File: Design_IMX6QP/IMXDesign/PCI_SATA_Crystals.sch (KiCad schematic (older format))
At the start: 15 parts, among them U1 MCIMX6QP5EVT

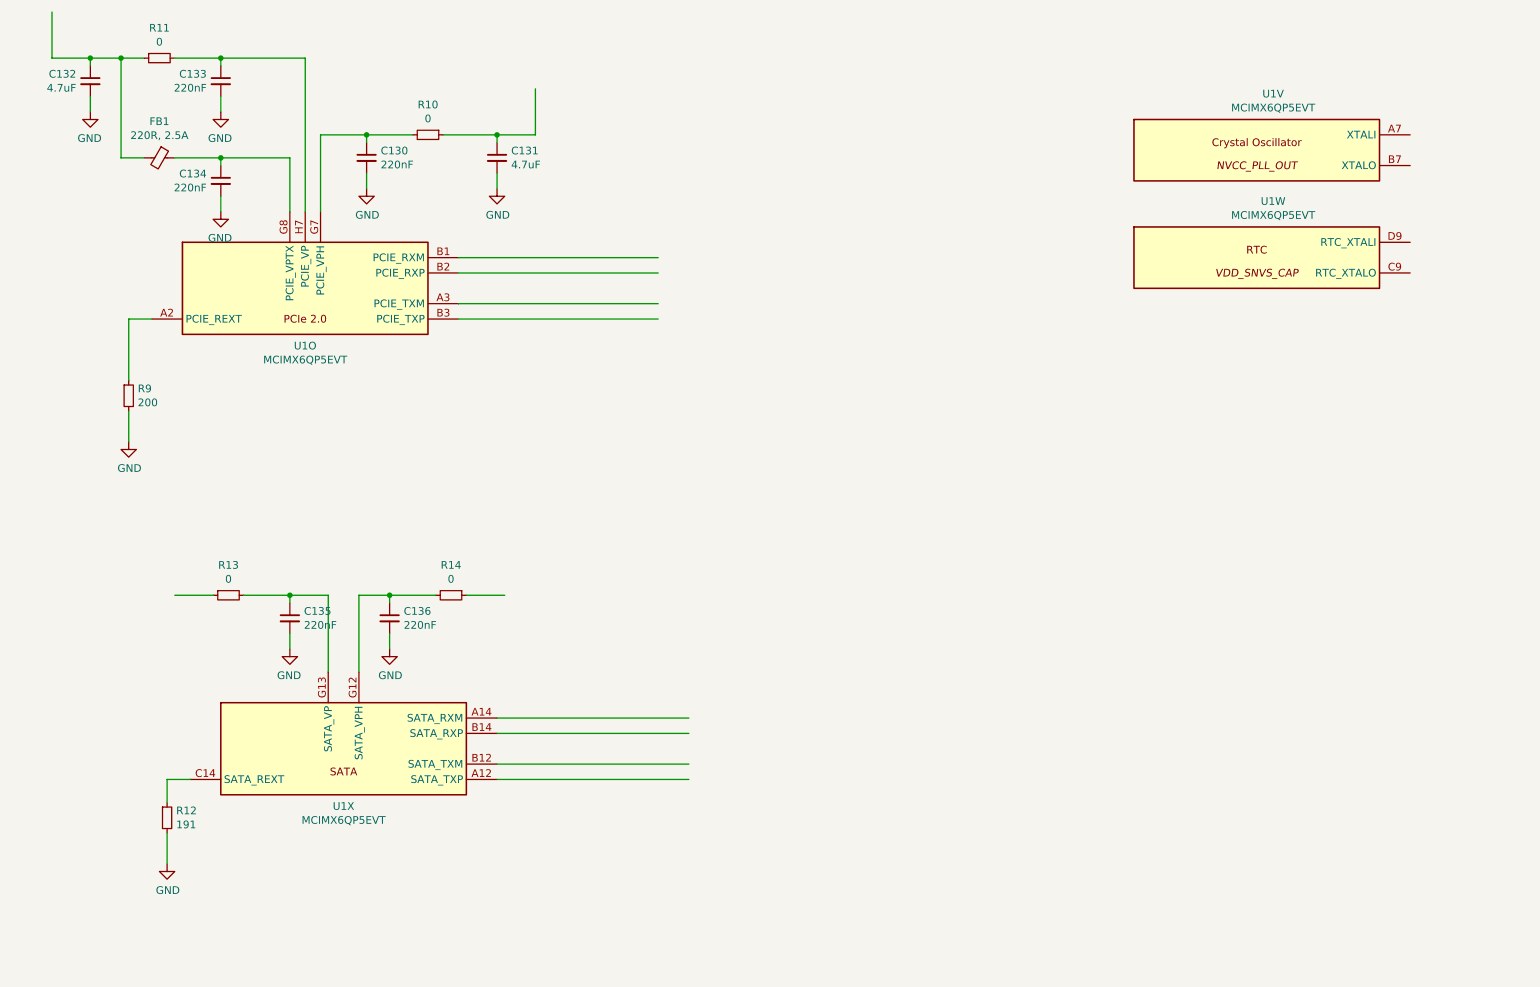
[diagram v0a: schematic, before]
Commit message: Update IMX6QP and IMX8MQ
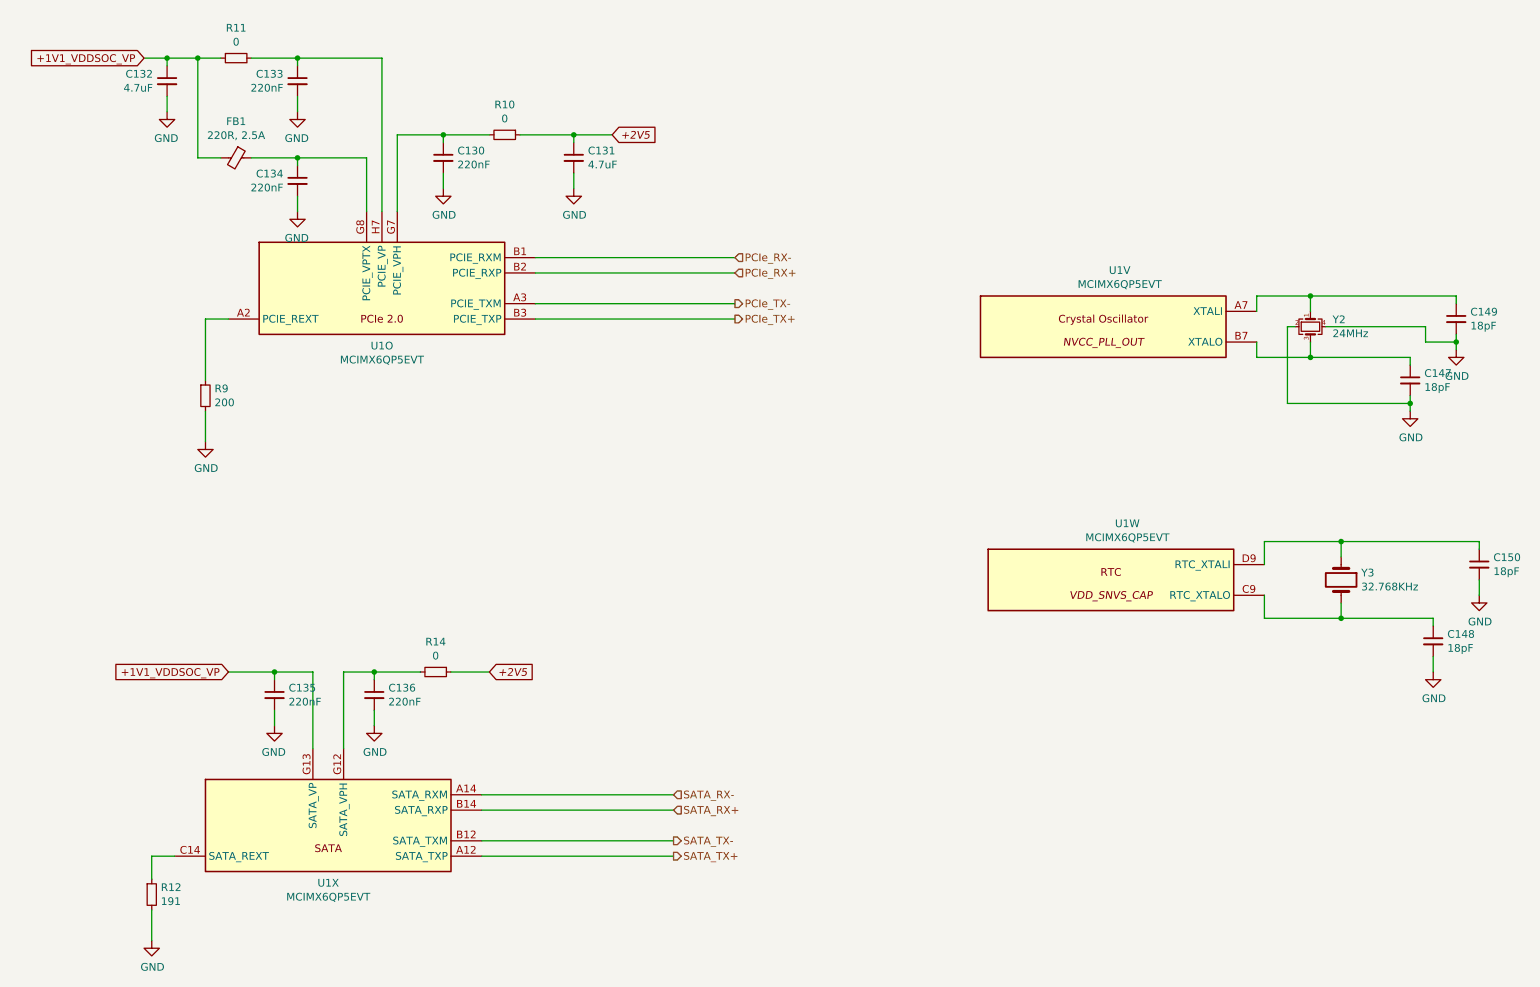
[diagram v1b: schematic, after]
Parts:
- removed R13: 0, Resistor_SMD:R_0201_0603Metric, symbol Device:R_Small
- added C147, C148, C149, C150: 18pF, Capacitor_SMD:C_0201_0603Metric, symbol Device:C_Small
- added Y2: 24MHz, Crystal:Crystal_SMD_2016-4Pin_2.0x1.6mm, symbol Device:Crystal_GND24_Small
- added Y3: 32.768KHz, Crystal:Crystal_SMD_2012-2Pin_2.0x1.2mm, symbol Device:Crystal
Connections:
- net labels added: +1V1_VDDSOC_VP, +2V5, PCIe_RX+, PCIe_RX-, PCIe_TX+, PCIe_TX-, SATA_RX+, SATA_RX-, SATA_TX+, SATA_TX-
- wire segments 54 -> 83
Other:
- moved on the sheet: C130, C131, C132, C133, C134, C135, C136, FB1, R10, R11, R12, R14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
